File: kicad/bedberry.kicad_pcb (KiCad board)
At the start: 4 copper layers, 100 x 100 mm, 88 parts, among them J1 629105150521, J2 SJ1-3533NG, J3 DIN-7, J4 DIN-7, J5 SJ1-3533NG, J6 SJ1-3533NG, J7 SJ1-3533NG, P1 RPi Zero 2 W, Q1 BC817, Q2 IRLML2246TRPBF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

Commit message: updated design
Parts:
- C10, C11, C12, C13, C14, C15, C16, C17, C18, C8, C9: value 100nF 0805 -> 100nF 0603
- C19: value 100uF 8mm TH -> 100uF 10mm TH; footprint Capacitor_THT:CP_Radial_D8.0mm_P3.50mm -> Capacitor_THT:CP_Radial_D10.0mm_P5.00mm
- C2, C20, C4: value 100nF 0805 -> 100nF 0603; footprint Capacitor_SMD:C_0805_2012Metric -> Capacitor_SMD:C_0603_1608Metric
- D1: value MP001251 -> KPFA-3010RGBC-11; footprint LED_SMD:LED_Avago_PLCC4_3.2x2.8mm_CW -> LED_SMD:LED_Kingbright_APFA3010_3x1.5mm_Horizontal
- J1: value 629105150521 -> USB Micro-B; footprint Connector_USB:USB_Micro-B_Molex_47346-0001 -> Connector_USB:USB_Micro-B_Amphenol_10118194_Horizontal
- JP1: footprint Connector_PinHeader_2.54mm:PinHeader_1x03_P2.54mm_Vertical_SMD_Pin1Left -> Connector_PinHeader_2.54mm:PinHeader_1x03_P2.54mm_Vertical
- Q2: value IRLML2246TRPBF -> MOSFET P-Ch
- R6, R9: value 12 -> 5.6
- R7: value 22k -> 10k
- RN5, RN6: value 270 -> 1.5k
- RN7, RN8: value 1k -> 1.5k
- U2: value MCP23017_SS -> MCP23017-E/SO
- moved R2 6.48 mm to (158.1, 161.4)
- moved D1 3.45 mm to (152.6, 159.9)
- moved R3 3.00 mm to (158.1, 158.4)
- moved R14 1.92 mm to (167.8, 114.5)
- moved R4 1.42 mm to (164.2, 159.9)
- moved R8 0.61 mm to (207.1, 114.4)
- moved C19 0.48 mm to (201.9, 122.0)
- moved C1 0.45 mm to (244.5, 133.9)
- moved J1 0.43 mm to (247.3, 125.5)
- moved JP1 0.37 mm to (175.1, 115.6)
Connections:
- D1 pad 1: +3V3 -> Net-(R2-Pad1)
- D1 pad 2: Net-(D1-Pad2) -> +3V3
- D1 pad 4: Net-(D1-Pad4) -> Net-(R4-Pad1)
- P1 pad 16: /GPIO23(GEN4) -> /GPIO23_RESET
- R12 pad 2: Net-(R12-Pad2) -> /GPIO23_RESET
- R2 pad 1: Net-(D1-Pad4) -> Net-(R2-Pad1)
- R4 pad 1: Net-(D1-Pad2) -> Net-(R4-Pad1)
- U2 pad 18: Net-(R12-Pad2) -> /GPIO23_RESET
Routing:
- net /USB_SHIELD: track 22.7 -> 0.00 mm
- net /GPIO23_RESET: track 0.00 -> 15.7 mm
- net Net-(R4-Pad1): track 0.00 -> 10.4 mm
- net Net-(D1-Pad2): track 9.47 -> 0.00 mm
- net /GPIO18_PWM0_LED_R: track 39.8 -> 49.2 mm
- net Net-(R12-Pad2): track 9.25 -> 0.00 mm
- net Net-(D1-Pad4): track 7.04 -> 0.00 mm
- net Net-(R2-Pad1): track 0.00 -> 4.60 mm
- net GND: track 9.63 -> 5.21 mm, vias 26 -> 31
- net +3V3: track 85.7 -> 81.8 mm, vias 25 -> 24
- net /GPIO13_PWM1_LED_G: track 45.4 -> 49.1 mm
- net Net-(JP1-Pad2): track 3.43 -> 6.97 mm
- net +5V: track 17.6 -> 20.6 mm
- net Net-(R3-Pad1): track 3.21 -> 4.61 mm
- net /GPIO5_AUX_OUT: track 77.7 -> 78.8 mm
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- added copper zone on F.Cu, net /USB_SHIELD
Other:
- board text added: "3.3V"
- board text added: "5V"

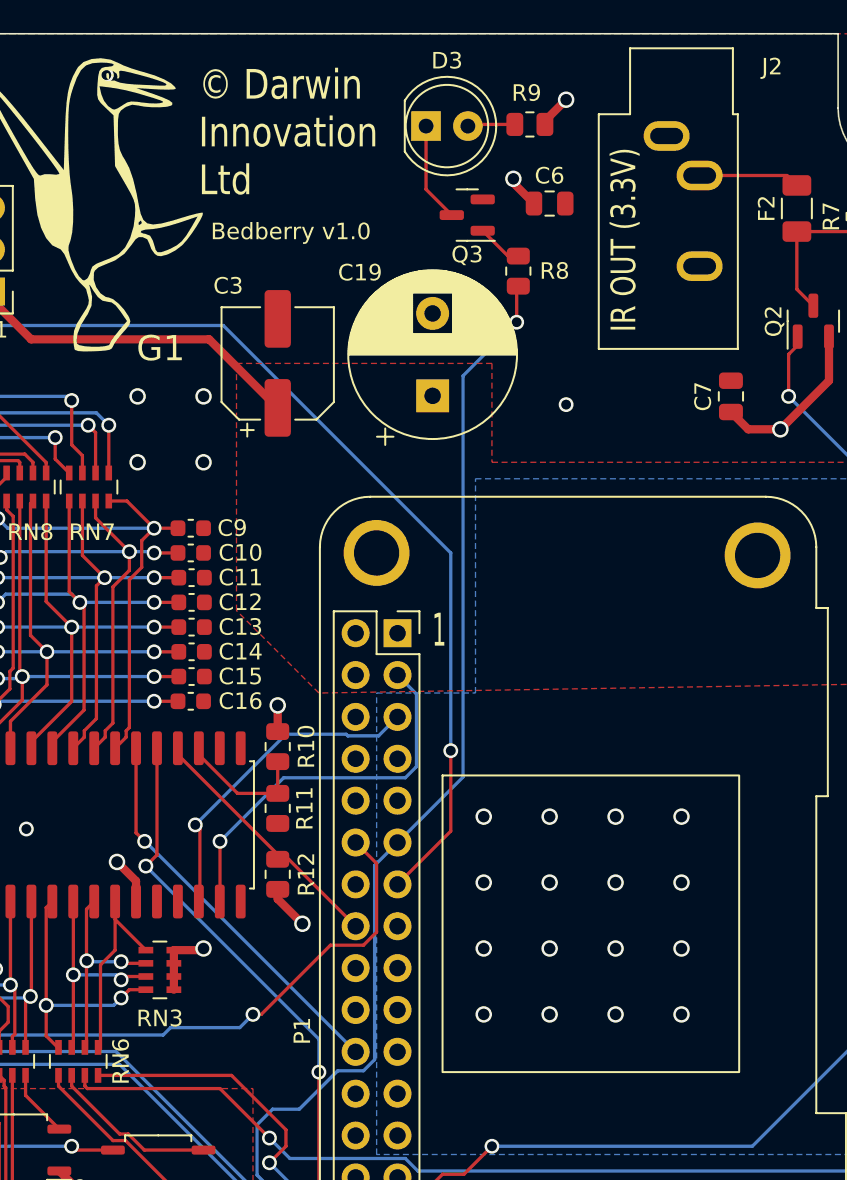
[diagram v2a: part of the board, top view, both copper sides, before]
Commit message: BOM changes; RPi thermal gap
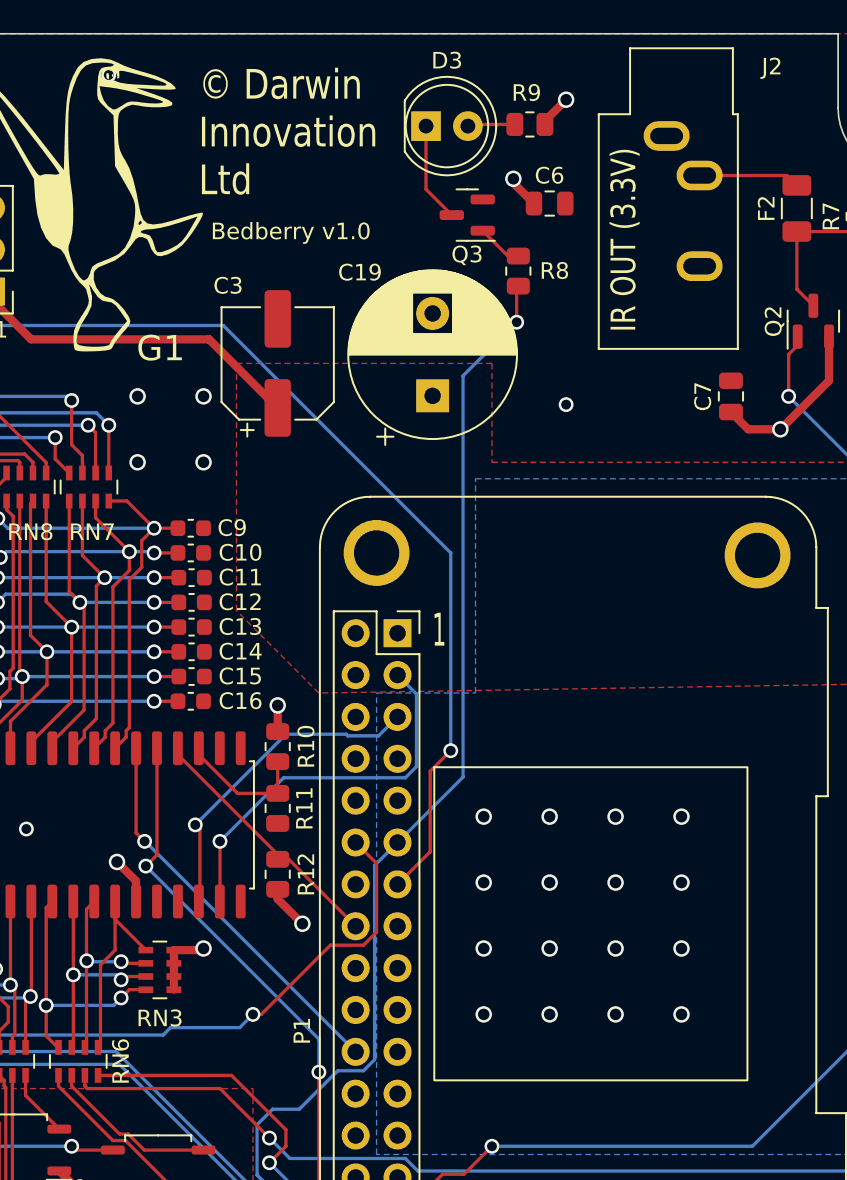
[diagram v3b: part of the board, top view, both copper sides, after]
